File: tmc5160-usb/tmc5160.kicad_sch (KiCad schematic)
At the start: 30 parts, among them J401 Molex_Pico-SPOX_Horizontal, J402 Molex_Pico-Clasp_Horizontal, U401 TMC5160A-WA, U402 MAX6816, X401 16MHz

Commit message: stepper-interface -> tmc5160-usb
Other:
- title: stepper-interface -> tmc5160-usb
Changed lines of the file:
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@@
   (paper "A4")
   (title_block
-    (title "stepper-interface")
+    (title "tmc5160-usb")
     (date "2024-05-10")
     (rev "1.0")
@@
     (pin "2")
     (instances
-      (project "stepper-interface"
+      (project "tmc5160-usb"
         (path "/df2b2e89-e055-4140-95de-f1df723db034/039ac378-5273-4081-85bf-9eb26cb5ed57"
           (reference "C411") (unit 1)
@@
     (pin "2")
     (instances
-      (project "stepper-interface"
+      (project "tmc5160-usb"
         (path "/df2b2e89-e055-4140-95de-f1df723db034/039ac378-5273-4081-85bf-9eb26cb5ed57"
           (reference "R406") (unit 1)
@@
     (pin "1")
     (instances
-      (project "stepper-interface"
+      (project "tmc5160-usb"
         (path "/df2b2e89-e055-4140-95de-f1df723db034/039ac378-5273-4081-85bf-9eb26cb5ed57"
           (reference "C408") (unit 1)
@@
     (pin "2")
     (instances
-      (project "stepper-interface"
+      (project "tmc5160-usb"
         (path "/df2b2e89-e055-4140-95de-f1df723db034/039ac378-5273-4081-85bf-9eb26cb5ed57"
           (reference "C409") (unit 1)
@@
     (pin "1")
     (instances
-      (project "stepper-interface"
+      (project "tmc5160-usb"
         (path "/df2b2e89-e055-4140-95de-f1df723db034/039ac378-5273-4081-85bf-9eb26cb5ed57"
           (reference "C406") (unit 1)
@@
     (pin "3")
     (instances
-      (project "stepper-interface"
+      (project "tmc5160-usb"
         (path "/df2b2e89-e055-4140-95de-f1df723db034/039ac378-5273-4081-85bf-9eb26cb5ed57"
           (reference "J401") (unit 1)
@@
     (pin "2")
     (instances
-      (project "stepper-interface"
+      (project "tmc5160-usb"
         (path "/df2b2e89-e055-4140-95de-f1df723db034/039ac378-5273-4081-85bf-9eb26cb5ed57"
           (reference "U402") (unit 1)
@@
     (pin "1")
     (instances
-      (project "stepper-interface"
+      (project "tmc5160-usb"
         (path "/df2b2e89-e055-4140-95de-f1df723db034/039ac378-5273-4081-85bf-9eb26cb5ed57"
           (reference "C401") (unit 1)
@@
     (pin "2")
     (instances
-      (project "stepper-interface"
+      (project "tmc5160-usb"
         (path "/df2b2e89-e055-4140-95de-f1df723db034/039ac378-5273-4081-85bf-9eb26cb5ed57"
           (reference "C410") (unit 1)
@@
     (pin "1")
     (instances
-      (project "stepper-interface"
+      (project "tmc5160-usb"
         (path "/df2b2e89-e055-4140-95de-f1df723db034/039ac378-5273-4081-85bf-9eb26cb5ed57"
           (reference "C413") (unit 1)
@@
     (pin "18")
     (instances
-      (project "stepper-interface"
+      (project "tmc5160-usb"
         (path "/df2b2e89-e055-4140-95de-f1df723db034/039ac378-5273-4081-85bf-9eb26cb5ed57"
           (reference "U401") (unit 1)
@@
     (pin "2")
     (instances
-      (project "stepper-interface"
+      (project "tmc5160-usb"
         (path "/df2b2e89-e055-4140-95de-f1df723db034/039ac378-5273-4081-85bf-9eb26cb5ed57"
           (reference "C402") (unit 1)
@@
     (pin "1")
     (instances
-      (project "stepper-interface"
+      (project "tmc5160-usb"
         (path "/df2b2e89-e055-4140-95de-f1df723db034/039ac378-5273-4081-85bf-9eb26cb5ed57"
           (reference "C415") (unit 1)
@@
     (pin "2")
     (instances
-      (project "stepper-interface"
+      (project "tmc5160-usb"
         (path "/df2b2e89-e055-4140-95de-f1df723db034/039ac378-5273-4081-85bf-9eb26cb5ed57"
           (reference "R402") (unit 1)
@@
     (pin "1")
     (instances
-      (project "stepper-interface"
+      (project "tmc5160-usb"
         (path "/df2b2e89-e055-4140-95de-f1df723db034/039ac378-5273-4081-85bf-9eb26cb5ed57"
           (reference "R404") (unit 1)
@@
     (pin "2")
     (instances
-      (project "stepper-interface"
+      (project "tmc5160-usb"
         (path "/df2b2e89-e055-4140-95de-f1df723db034/039ac378-5273-4081-85bf-9eb26cb5ed57"
           (reference "D401") (unit 1)
@@
     (pin "1")
     (instances
-      (project "stepper-interface"
+      (project "tmc5160-usb"
         (path "/df2b2e89-e055-4140-95de-f1df723db034/039ac378-5273-4081-85bf-9eb26cb5ed57"
           (reference "#FLG0401") (unit 1)
@@
     (pin "2")
     (instances
-      (project "stepper-interface"
+      (project "tmc5160-usb"
         (path "/df2b2e89-e055-4140-95de-f1df723db034/039ac378-5273-4081-85bf-9eb26cb5ed57"
           (reference "X401") (unit 1)
@@
     (pin "1")
     (instances
-      (project "stepper-interface"
+      (project "tmc5160-usb"
         (path "/df2b2e89-e055-4140-95de-f1df723db034/039ac378-5273-4081-85bf-9eb26cb5ed57"
           (reference "J402") (unit 1)
@@
     (pin "2")
     (instances
-      (project "stepper-interface"
+      (project "tmc5160-usb"
         (path "/df2b2e89-e055-4140-95de-f1df723db034/039ac378-5273-4081-85bf-9eb26cb5ed57"
           (reference "R403") (unit 1)
@@
     (pin "1")
     (instances
-      (project "stepper-interface"
+      (project "tmc5160-usb"
         (path "/df2b2e89-e055-4140-95de-f1df723db034/039ac378-5273-4081-85bf-9eb26cb5ed57"
           (reference "C405") (unit 1)
@@
     (pin "2")
     (instances
-      (project "stepper-interface"
+      (project "tmc5160-usb"
         (path "/df2b2e89-e055-4140-95de-f1df723db034/039ac378-5273-4081-85bf-9eb26cb5ed57"
           (reference "C416") (unit 1)
@@
     (pin "2")
     (instances
-      (project "stepper-interface"
+      (project "tmc5160-usb"
         (path "/df2b2e89-e055-4140-95de-f1df723db034/039ac378-5273-4081-85bf-9eb26cb5ed57"
           (reference "C412") (unit 1)
@@
     (pin "2")
     (instances
-      (project "stepper-interface"
+      (project "tmc5160-usb"
         (path "/df2b2e89-e055-4140-95de-f1df723db034/039ac378-5273-4081-85bf-9eb26cb5ed57"
           (reference "R407") (unit 1)
@@
     (pin "2")
     (instances
-      (project "stepper-interface"
+      (project "tmc5160-usb"
         (path "/df2b2e89-e055-4140-95de-f1df723db034/039ac378-5273-4081-85bf-9eb26cb5ed57"
           (reference "R401") (unit 1)
@@
     (pin "1")
     (instances
-      (project "stepper-interface"
+      (project "tmc5160-usb"
         (path "/df2b2e89-e055-4140-95de-f1df723db034/039ac378-5273-4081-85bf-9eb26cb5ed57"
           (reference "C404") (unit 1)
@@
     (pin "1")
     (instances
-      (project "stepper-interface"
+      (project "tmc5160-usb"
         (path "/df2b2e89-e055-4140-95de-f1df723db034/039ac378-5273-4081-85bf-9eb26cb5ed57"
           (reference "R405") (unit 1)
@@
     (pin "1")
     (instances
-      (project "stepper-interface"
+      (project "tmc5160-usb"
         (path "/df2b2e89-e055-4140-95de-f1df723db034/039ac378-5273-4081-85bf-9eb26cb5ed57"
           (reference "C407") (unit 1)
@@
     (pin "1")
     (instances
-      (project "stepper-interface"
+      (project "tmc5160-usb"
         (path "/df2b2e89-e055-4140-95de-f1df723db034/039ac378-5273-4081-85bf-9eb26cb5ed57"
           (reference "C414") (unit 1)
@@
     (pin "1")
     (instances
-      (project "stepper-interface"
+      (project "tmc5160-usb"
         (path "/df2b2e89-e055-4140-95de-f1df723db034/039ac378-5273-4081-85bf-9eb26cb5ed57"
           (reference "C403") (unit 1)
@@
     (pin "1")
     (instances
-      (project "stepper-interface"
+      (project "tmc5160-usb"
         (path "/df2b2e89-e055-4140-95de-f1df723db034/039ac378-5273-4081-85bf-9eb26cb5ed57"
           (reference "C417") (unit 1)
@@
     )
     (instances
-      (project "stepper-interface"
+      (project "tmc5160-usb"
         (path "/df2b2e89-e055-4140-95de-f1df723db034/039ac378-5273-4081-85bf-9eb26cb5ed57" (page "8"))
       )
@@
     )
     (instances
-      (project "stepper-interface"
+      (project "tmc5160-usb"
         (path "/df2b2e89-e055-4140-95de-f1df723db034/039ac378-5273-4081-85bf-9eb26cb5ed57" (page "5"))
       )
@@
     )
     (instances
-      (project "stepper-interface"
+      (project "tmc5160-usb"
         (path "/df2b2e89-e055-4140-95de-f1df723db034/039ac378-5273-4081-85bf-9eb26cb5ed57" (page "9"))
       )
@@
     )
     (instances
-      (project "stepper-interface"
+      (project "tmc5160-usb"
         (path "/df2b2e89-e055-4140-95de-f1df723db034/039ac378-5273-4081-85bf-9eb26cb5ed57" (page "11"))
       )
@@
     )
     (instances
-      (project "stepper-interface"
+      (project "tmc5160-usb"
         (path "/df2b2e89-e055-4140-95de-f1df723db034/039ac378-5273-4081-85bf-9eb26cb5ed57" (page "7"))
       )
@@
     )
     (instances
-      (project "stepper-interface"
+      (project "tmc5160-usb"
         (path "/df2b2e89-e055-4140-95de-f1df723db034/039ac378-5273-4081-85bf-9eb26cb5ed57" (page "12"))
       )
@@
     )
     (instances
-      (project "stepper-interface"
+      (project "tmc5160-usb"
         (path "/df2b2e89-e055-4140-95de-f1df723db034/039ac378-5273-4081-85bf-9eb26cb5ed57" (page "6"))
       )
@@
     )
     (instances
-      (project "stepper-interface"
+      (project "tmc5160-usb"
         (path "/df2b2e89-e055-4140-95de-f1df723db034/039ac378-5273-4081-85bf-9eb26cb5ed57" (page "10"))
       )

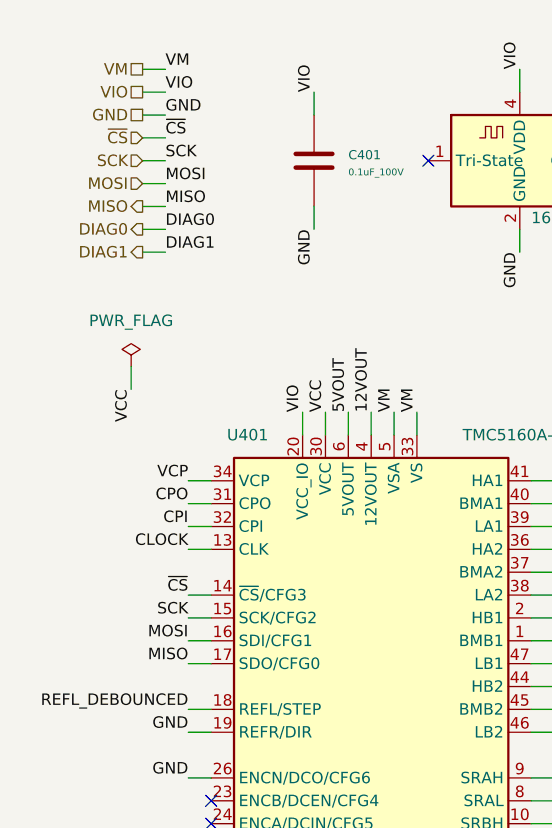
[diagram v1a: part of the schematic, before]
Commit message: mosi -> copi, miso -> cipo
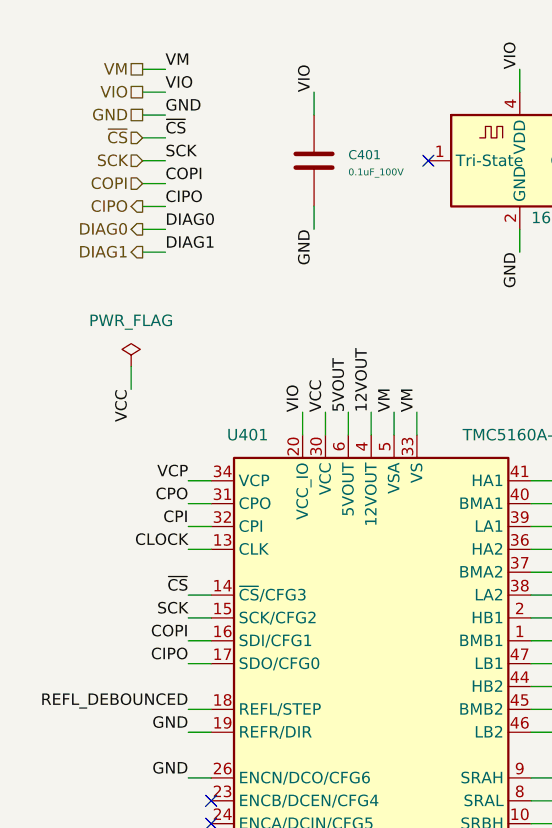
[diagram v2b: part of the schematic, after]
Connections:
- net MISO renamed CIPO
- net MOSI renamed COPI
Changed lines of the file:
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@@
     (effects (font (size 1.27 1.27)) (justify right bottom))
   )
-  (label "MOSI" (at 34.29 93.98 180) (fields_autoplaced)
+  (label "COPI" (at 34.29 93.98 180) (fields_autoplaced)
     (effects (font (size 1.27 1.27)) (justify right bottom))
   )
@@
     (effects (font (size 1.27 1.27)) (justify left bottom))
   )
-  (label "MISO" (at 34.29 96.52 180) (fields_autoplaced)
+  (label "CIPO" (at 34.29 96.52 180) (fields_autoplaced)
     (effects (font (size 1.27 1.27)) (justify right bottom))
   )
@@
     (effects (font (size 1.27 1.27)) (justify right bottom))
   )
-  (label "MISO" (at 31.75 45.72 0) (fields_autoplaced)
+  (label "CIPO" (at 31.75 45.72 0) (fields_autoplaced)
     (effects (font (size 1.27 1.27)) (justify left bottom))
   )
@@
     (effects (font (size 1.27 1.27)) (justify left bottom))
   )
-  (label "MOSI" (at 31.75 43.18 0) (fields_autoplaced)
+  (label "COPI" (at 31.75 43.18 0) (fields_autoplaced)
     (effects (font (size 1.27 1.27)) (justify left bottom))
   )
@@
     (effects (font (size 1.27 1.27)) (justify right))
   )
-  (hierarchical_label "MISO" (shape output) (at 29.21 45.72 180) (fields_autoplaced)
-    (effects (font (size 1.27 1.27)) (justify right))
-  )
-  (hierarchical_label "MOSI" (shape input) (at 29.21 43.18 180) (fields_autoplaced)
-    (effects (font (size 1.27 1.27)) (justify right))
-  )
+  (hierarchical_label "CIPO" (shape output) (at 29.21 45.72 180) (fields_autoplaced)
+    (effects (font (size 1.27 1.27)) (justify right))
+  )
+  (hierarchical_label "COPI" (shape input) (at 29.21 43.18 180) (fields_autoplaced)
+    (effects (font (size 1.27 1.27)) (justify right))
+  )
